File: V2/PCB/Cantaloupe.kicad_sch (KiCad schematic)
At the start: 123 parts, among them J1 USB_In, J2 OLED, J3 Link, J4 Debug, J5 Trackpad, Q1 2N7002, Q2 AO3401A, SW1 MX, SW10 MX, SW11 MX, SW12 MX, SW13 MX, SW14 MX, SW15 MX, SW16 MX, SW17 MX, SW18 MX, SW19 MX, SW2 MX, SW20 MX, SW21 MX, SW22 MX, SW23 MX, SW24 MX, SW25 MX, SW26 MX, SW27 MX, SW28 MX, SW29 MX, SW3 MX, SW30 MX, SW31 Encoder, SW32 MX, SW4 MX, SW5 MX, SW6 MX, SW7 MX, SW8 MX, SW9 MX, U1 STM32F4x1CxUx, U2 SRV0504, U3 SRV0504, U4 XC6206P332MR, U5 LMV321, Y1 8MHz

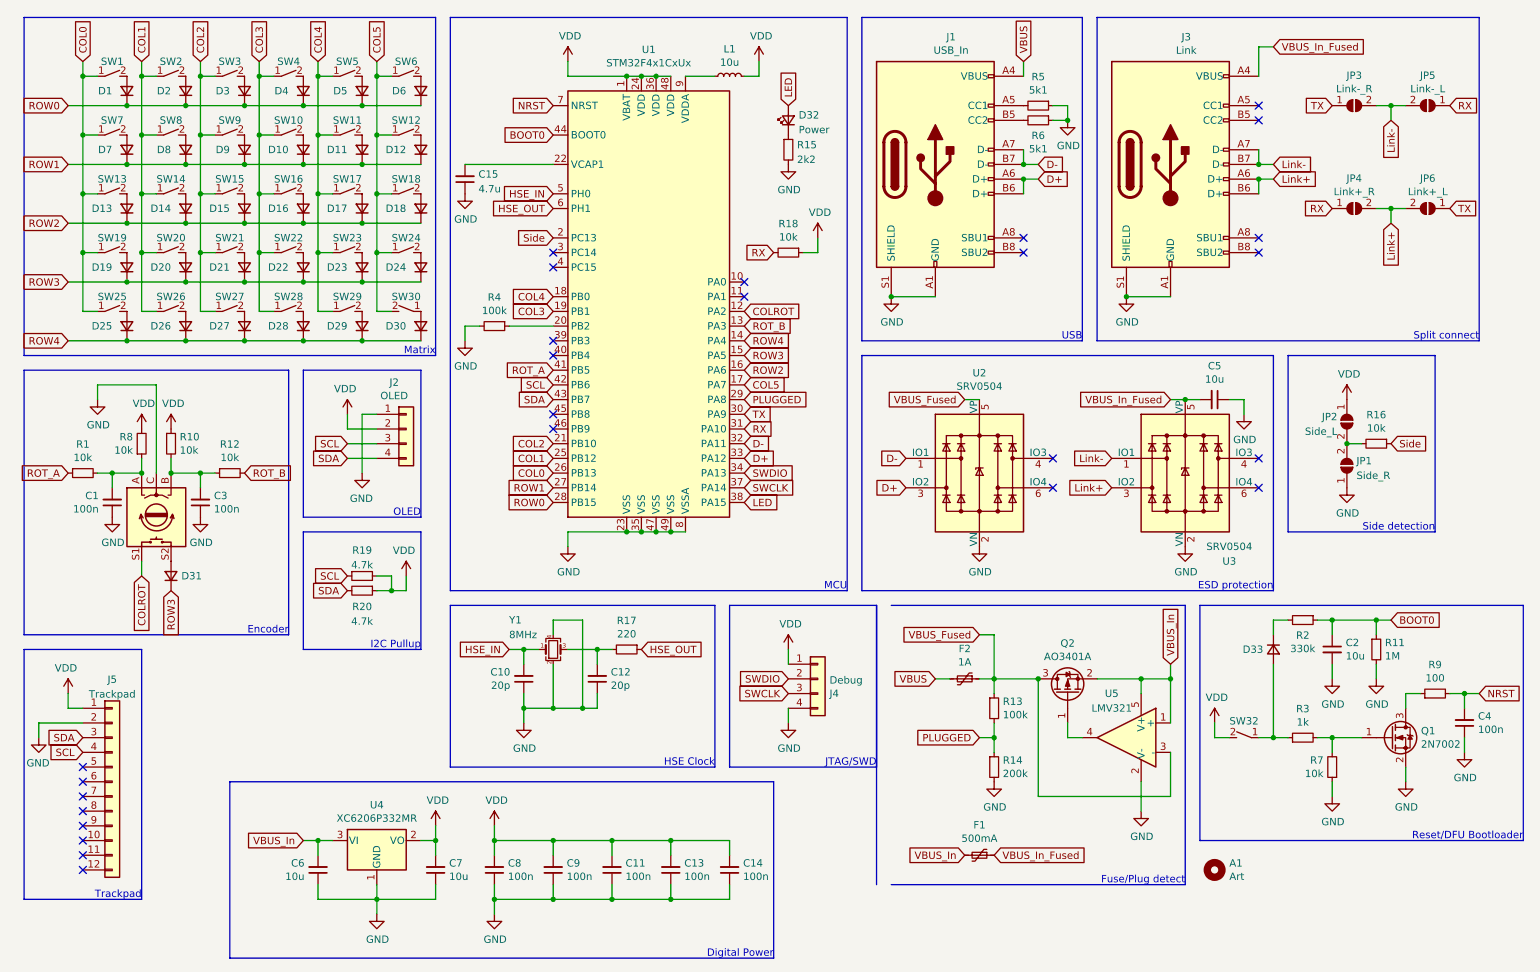
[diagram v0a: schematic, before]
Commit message: Revert "Tentative V2.1 update"
This reverts commit 42b4223a0f1e602d13e2d92696f419f95c71691f.
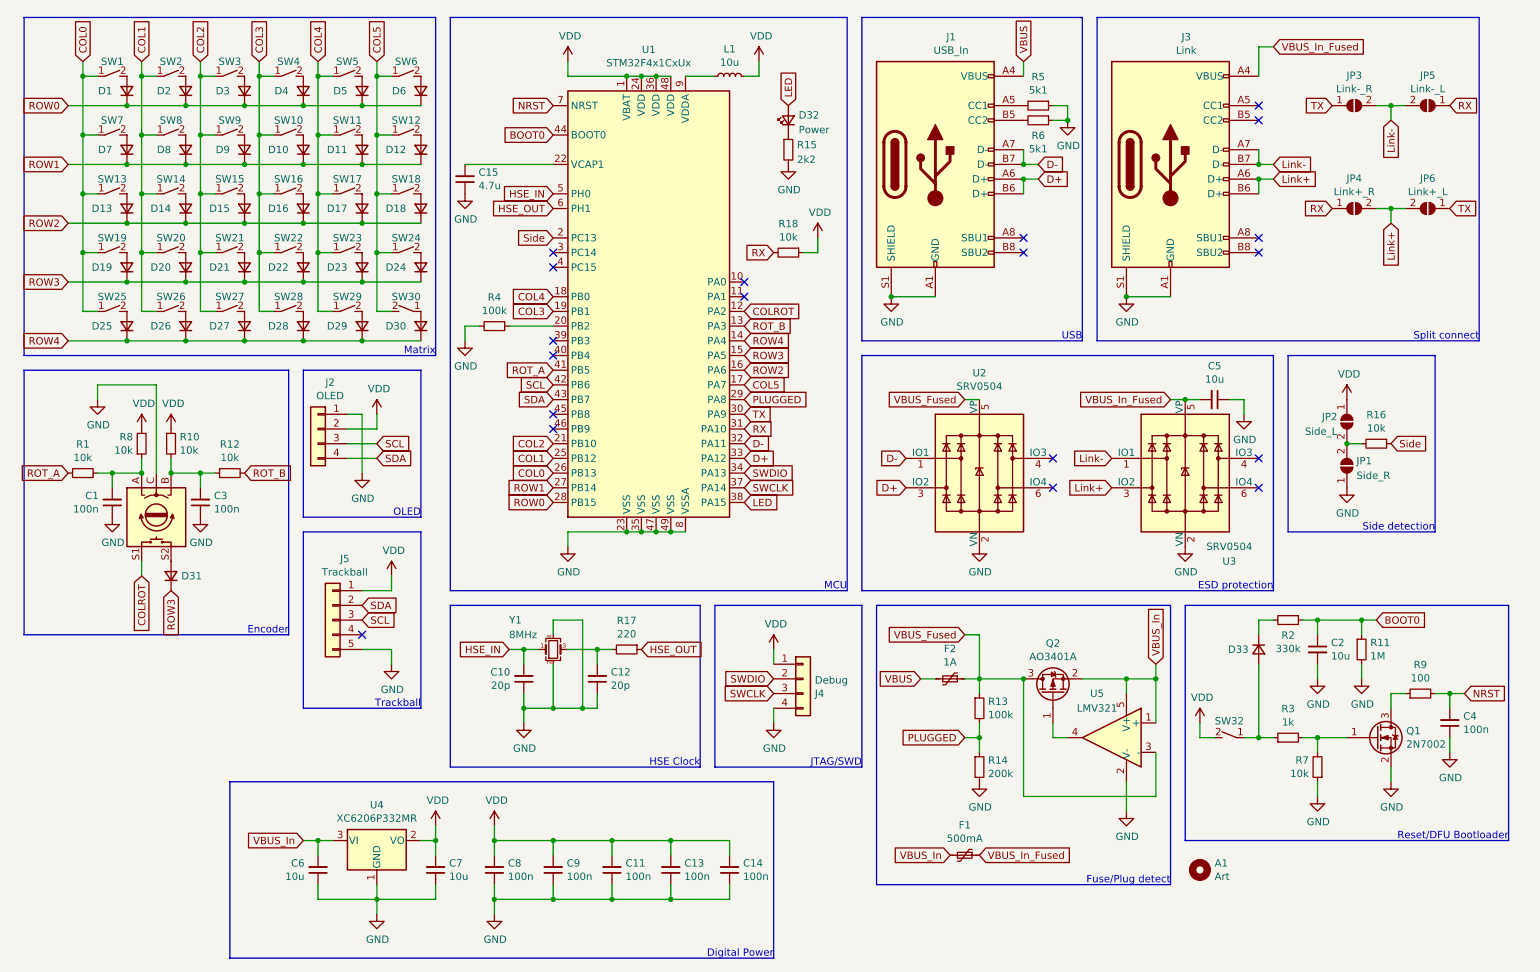
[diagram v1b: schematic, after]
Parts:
- removed J5: Trackpad, Ariamelon:FPC-SMD_FPC05012-09200-.5mm-rev, symbol Connector_Generic:Conn_01x12
- removed R19, R20: 4.7k, Resistor_SMD:R_0603_1608Metric, symbol Device:R_Small
- added J5: Trackball, Ariamelon:pimoroni_trackball_flippable, symbol Connector_Generic:Conn_01x05
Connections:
- net GND: now also J5.5 (Pin_5)
- net SCL: now also J5.3 (Pin_3)
- net SDA: now also J5.2 (Pin_2)
- net VDD: now also J5.1 (Pin_1)
- no-connect marks 26 -> 19
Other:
- note added: "Trackball"
- note removed: "I2C Pullup"
- note removed: "Trackpad"
- moved on the sheet: A1, C2, C4, D33, F1, F2, J2, J4, Q1, Q2, R11, R13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

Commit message: Tentative V2.1 update
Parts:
- removed J5: Trackball, Ariamelon:pimoroni_trackball_flippable, symbol Connector_Generic:Conn_01x05
- added J5: Trackpad, Ariamelon:FPC-SMD_FPC05012-09200-.5mm-rev, symbol Connector_Generic:Conn_01x12
- added R19, R20: 4.7k, Resistor_SMD:R_0603_1608Metric, symbol Device:R_Small
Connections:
- net GND: now also J5.2 (Pin_2)
- net SCL: now also J5.4 (Pin_4), R19.1
- net SDA: now also J5.3 (Pin_3), R20.2
- net VDD: now also J5.1 (Pin_1), R19.2, R20.1
- no-connect marks 19 -> 26
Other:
- note added: "I2C Pullup"
- note added: "Trackpad"
- note removed: "Trackball"
- moved on the sheet: A1, C2, C4, D33, F1, F2, J2, J4, Q1, Q2, R11, R13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
